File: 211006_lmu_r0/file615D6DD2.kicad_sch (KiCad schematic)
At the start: 26 parts, among them J11 Conn_ARM_JTAG_SWD_10, J12 Conn_01x03, SW1 SW_Push, SW2 SW_SPST, U9 STM32F103C8Tx, Y1 16MHz

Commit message: Updated lmu project with relative library paths and fixed broken symbols
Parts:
- FB1: symbol Device:Ferrite_Bead -> Device:FerriteBead
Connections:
- net +3V3: now reaches C183.1, C184.1, C185.1, C186.1, FB1.1, U9.1 (VBAT), U9.24 (VDD), U9.36 (VDD), U9.48 (VDD)
- net +3V3: now also J11.1 (VTref), R247.1
- net GND: now reaches U9.23 (VSS), U9.35 (VSS), U9.47 (VSS), U9.8 (VSSA)
- net GND: now also C182.2, C183.2, C184.2, C185.2, C186.2, D40.1 (K), D41.1 (K), D42.1 (K), D43.1 (K), D44.1 (K), J11.3 (GND), J11.5 (GND), J11.9 (GNDDetect), J12.3 (Pin_3), SW1.1, SW2.1 (A), Y1.2, Y1.3
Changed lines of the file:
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@@
     (pin "9")
   )
-  (symbol (lib_id "Device:Ferrite_Bead") (at 179.07 60.96 270) (unit 1)
+  (symbol (lib_id "Device:FerriteBead") (at 179.07 60.96 270) (unit 1)
     (in_bom yes) (on_board yes)
     (property "Reference" "FB1" (id 0) (at 180.34 64.77 90))
@@
       (effects (font (size 1.27 1.27)) hide)
     )
+    (pin "1")
   )
   (symbol (lib_id "gnd_iso:GND_ISO") (at 74.93 144.78 0) (unit 1)
@@
       (effects (font (size 1.27 1.27)) hide)
     )
+    (pin "1")
   )
   (symbol (lib_id "gnd_iso:GND_ISO") (at 66.04 144.78 0) (unit 1)
@@
       (effects (font (size 1.27 1.27)) hide)
     )
+    (pin "1")
   )
   (symbol (lib_id "gnd_iso:GND_ISO") (at 55.88 144.78 0) (unit 1)
@@
       (effects (font (size 1.27 1.27)) hide)
     )
+    (pin "1")
   )
   (symbol (lib_id "gnd_iso:GND_ISO") (at 45.72 144.78 0) (unit 1)
@@
       (effects (font (size 1.27 1.27)) hide)
     )
+    (pin "1")
   )
   (symbol (lib_id "gnd_iso:GND_ISO") (at 120.65 77.47 0) (unit 1)
@@
       (effects (font (size 1.27 1.27)) hide)
     )
+    (pin "1")
   )
   (symbol (lib_id "gnd_iso:GND_ISO") (at 107.95 77.47 0) (unit 1)
@@
       (effects (font (size 1.27 1.27)) hide)
     )
+    (pin "1")
   )
   (symbol (lib_id "gnd_iso:GND_ISO") (at 85.09 76.2 0) (unit 1)
@@
       (effects (font (size 1.27 1.27)) hide)
     )
+    (pin "1")
   )
   (symbol (lib_id "gnd_iso:GND_ISO") (at 95.25 81.28 0) (unit 1)
@@
       (effects (font (size 1.27 1.27)) hide)
     )
+    (pin "1")
   )
   (symbol (lib_id "gnd_iso:GND_ISO") (at 191.77 64.77 0) (unit 1)
@@
       (effects (font (size 1.27 1.27)) hide)
     )
+    (pin "1")
   )
   (symbol (lib_id "gnd_iso:GND_ISO") (at 200.66 64.77 0) (unit 1)
@@
       (effects (font (size 1.27 1.27)) hide)
     )
+    (pin "1")
   )
   (symbol (lib_id "gnd_iso:GND_ISO") (at 209.55 64.77 0) (unit 1)
@@
       (effects (font (size 1.27 1.27)) hide)
     )
+    (pin "1")
   )
   (symbol (lib_id "gnd_iso:GND_ISO") (at 218.44 64.77 0) (unit 1)
@@
       (effects (font (size 1.27 1.27)) hide)
     )
+    (pin "1")
   )
   (symbol (lib_id "gnd_iso:GND_ISO") (at 34.29 52.07 0) (unit 1)
@@
       (effects (font (size 1.27 1.27)) hide)
     )
+    (pin "1")
   )
   (symbol (lib_id "gnd_iso:GND_ISO") (at 71.12 30.48 0) (unit 1)
@@
       (effects (font (size 1.27 1.27)) hide)
     )
+    (pin "1")
   )
   (symbol (lib_id "+3v3_iso:+3V3_ISO") (at 218.44 57.15 0) (unit 1)
@@
       (effects (font (size 1.27 1.27)) hide)
     )
+    (pin "1")
   )
   (symbol (lib_id "+3v3_iso:+3V3_ISO") (at 85.09 58.42 0) (unit 1)
@@
       (effects (font (size 1.27 1.27)) hide)
     )
+    (pin "1")
   )
   (symbol (lib_id "+3v3_iso:+3V3_ISO") (at 34.29 21.59 0) (unit 1)
@@
       (effects (font (size 1.27 1.27)) hide)
     )
+    (pin "1")
   )
   (symbol (lib_id "Device:C") (at 200.66 60.96 0) (unit 1)
@@
       (effects (font (size 1.27 1.27)) hide)
     )
+    (pin "1")
   )
 )

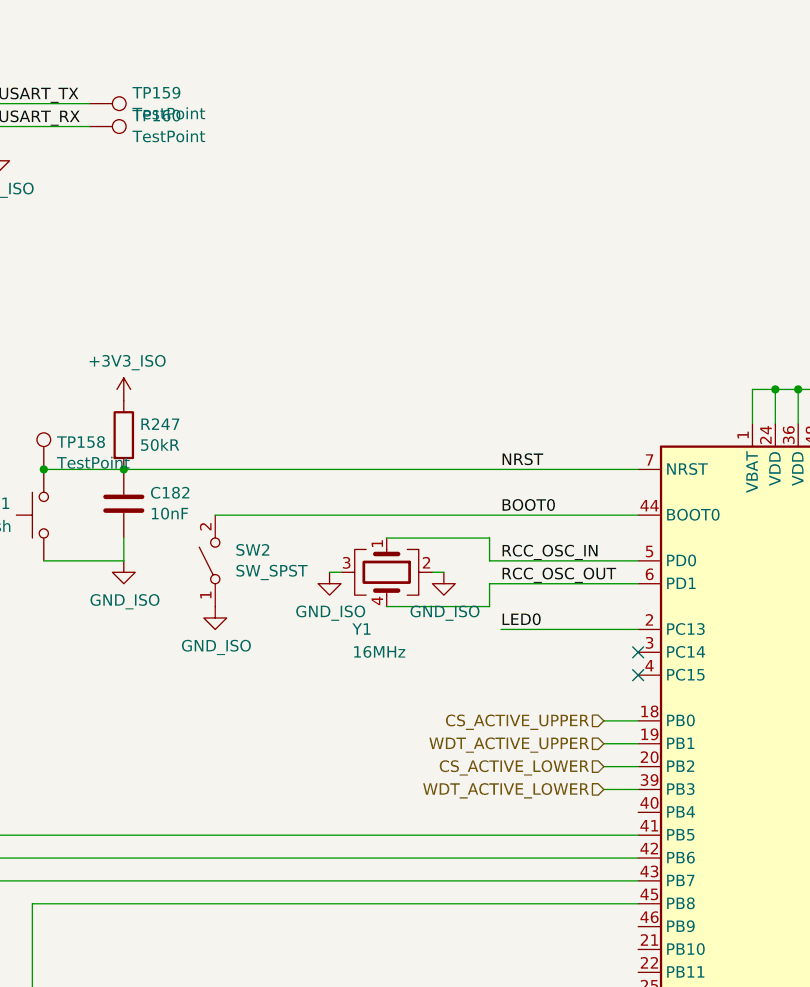
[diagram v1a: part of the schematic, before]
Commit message: Updated some components to make sourcing easier
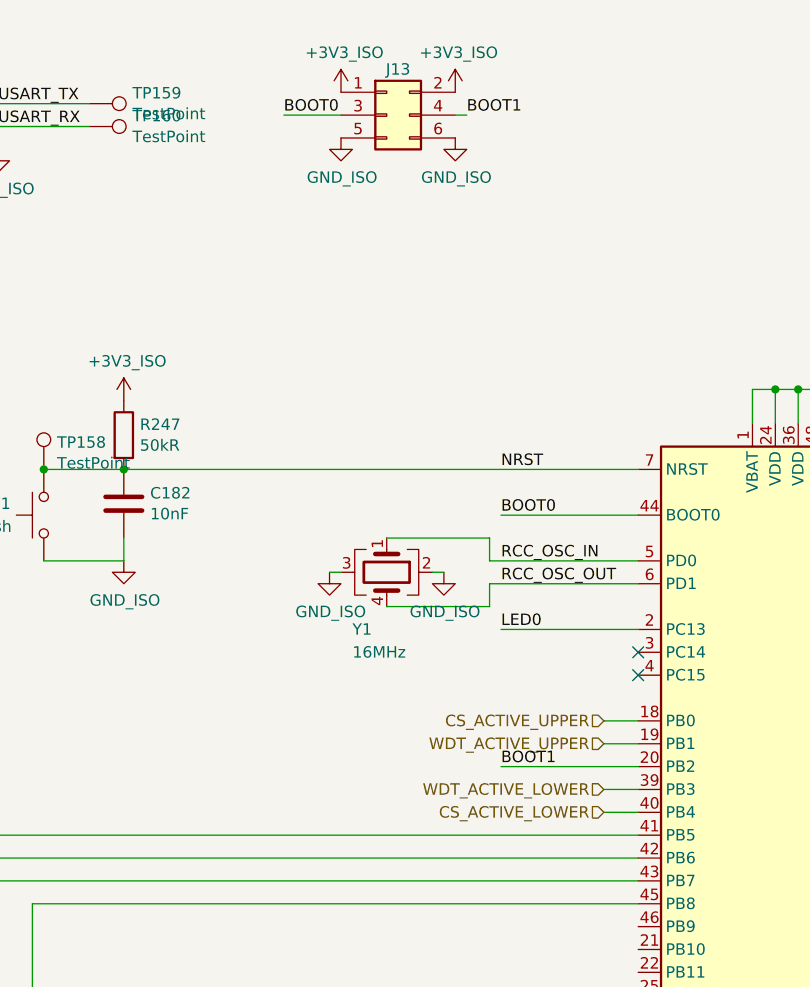
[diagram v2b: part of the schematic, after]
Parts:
- removed SW2: SW_SPST, Button_Switch_SMD:SW_DIP_SPSTx01_Slide_9.78x4.72mm_W8.61mm_P2.54mm, symbol Switch:SW_SPST
- added J13: Conn_02x03_Odd_Even, Connector_PinHeader_2.54mm:PinHeader_2x03_P2.54mm_Vertical, symbol Connector_Generic:Conn_02x03_Odd_Even
- C182, C183, C184, C185, C186, J12, R242, R243, R244, R245, R246, R247: Manufacturer (none) -> -; Part Number (none) -> -
- J11: Manufacturer (none) -> Samtec; Part Number (none) -> FTSH-105-01-L-DV-007-K
- SW1: footprint Button_Switch_SMD:SW_SPST_Omron_B3FS-100xP -> Button_Switch_SMD:SW_SPST_SKQG_WithStem; Manufacturer (none) -> XKB; Part Number (none) -> TS-1187A-C-D-B
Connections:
- net +3V3: now also J13.1 (Pin_1), J13.2 (Pin_2)
- net BOOT0: now also J13.3 (Pin_3)
- net CS_ACTIVE_LOWER: now also U9.40 (PB4); no longer U9.20 (PB2)
- net GND: now also J13.5 (Pin_5), J13.6 (Pin_6)
- new net BOOT1: J13.4 (Pin_4), U9.20 (PB2)

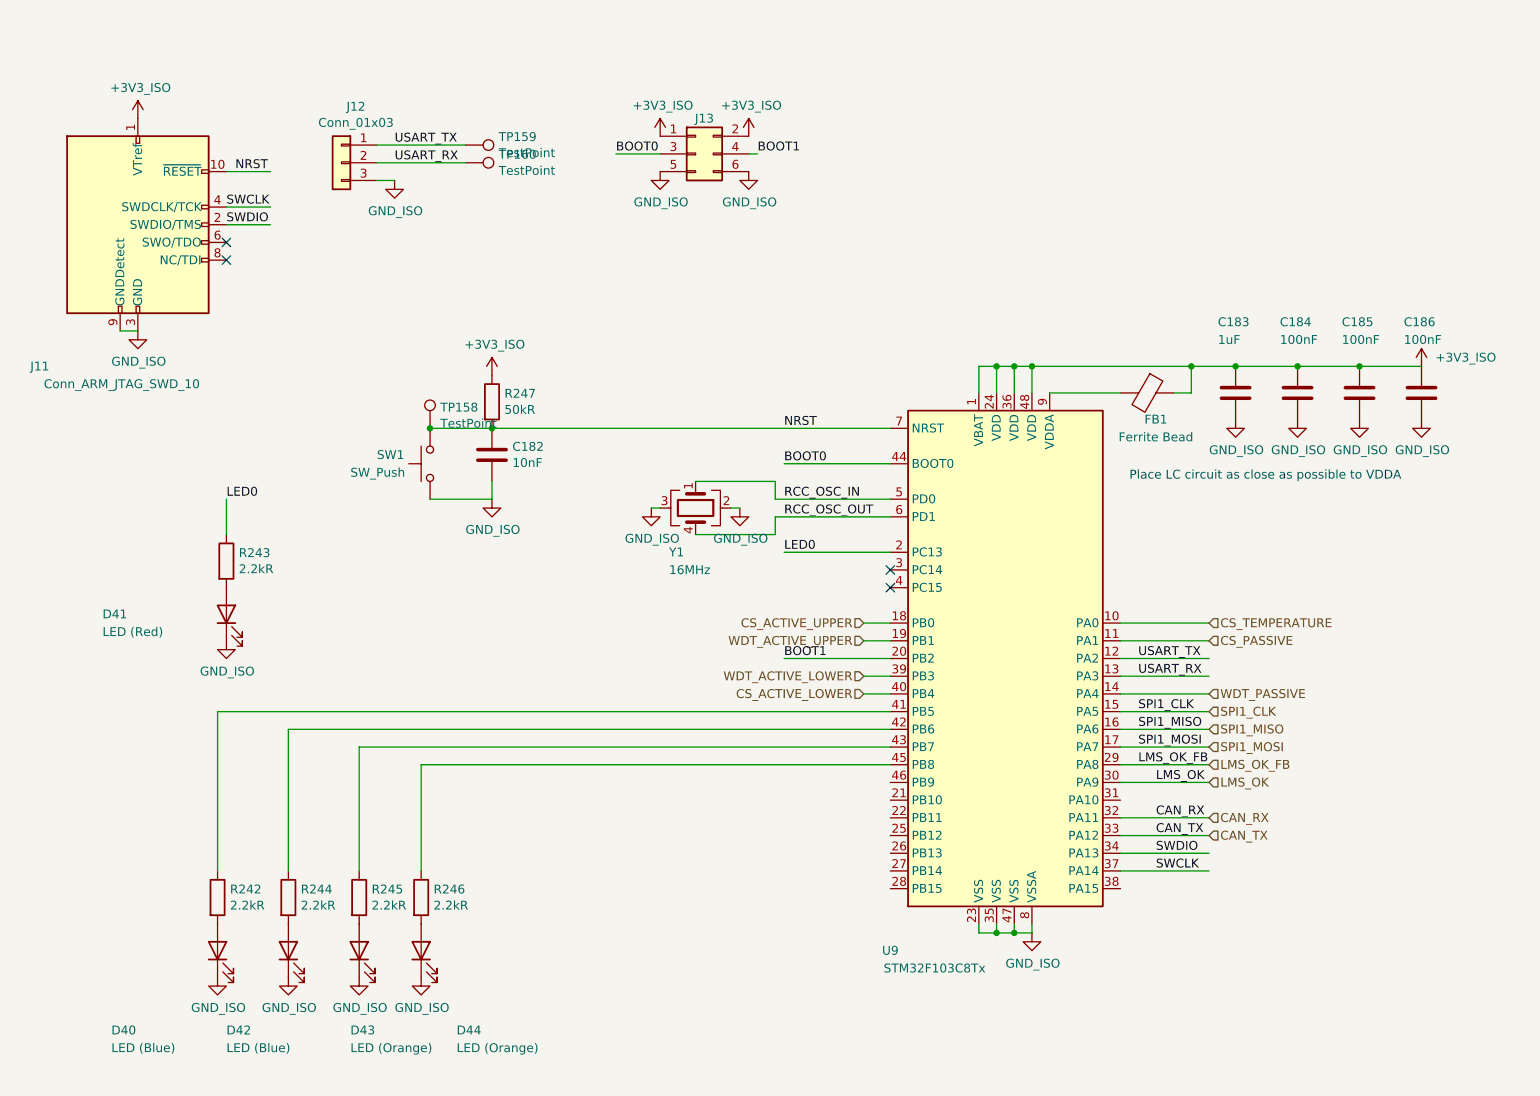
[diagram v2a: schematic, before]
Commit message: fixed footprints for headers, started planning out zones
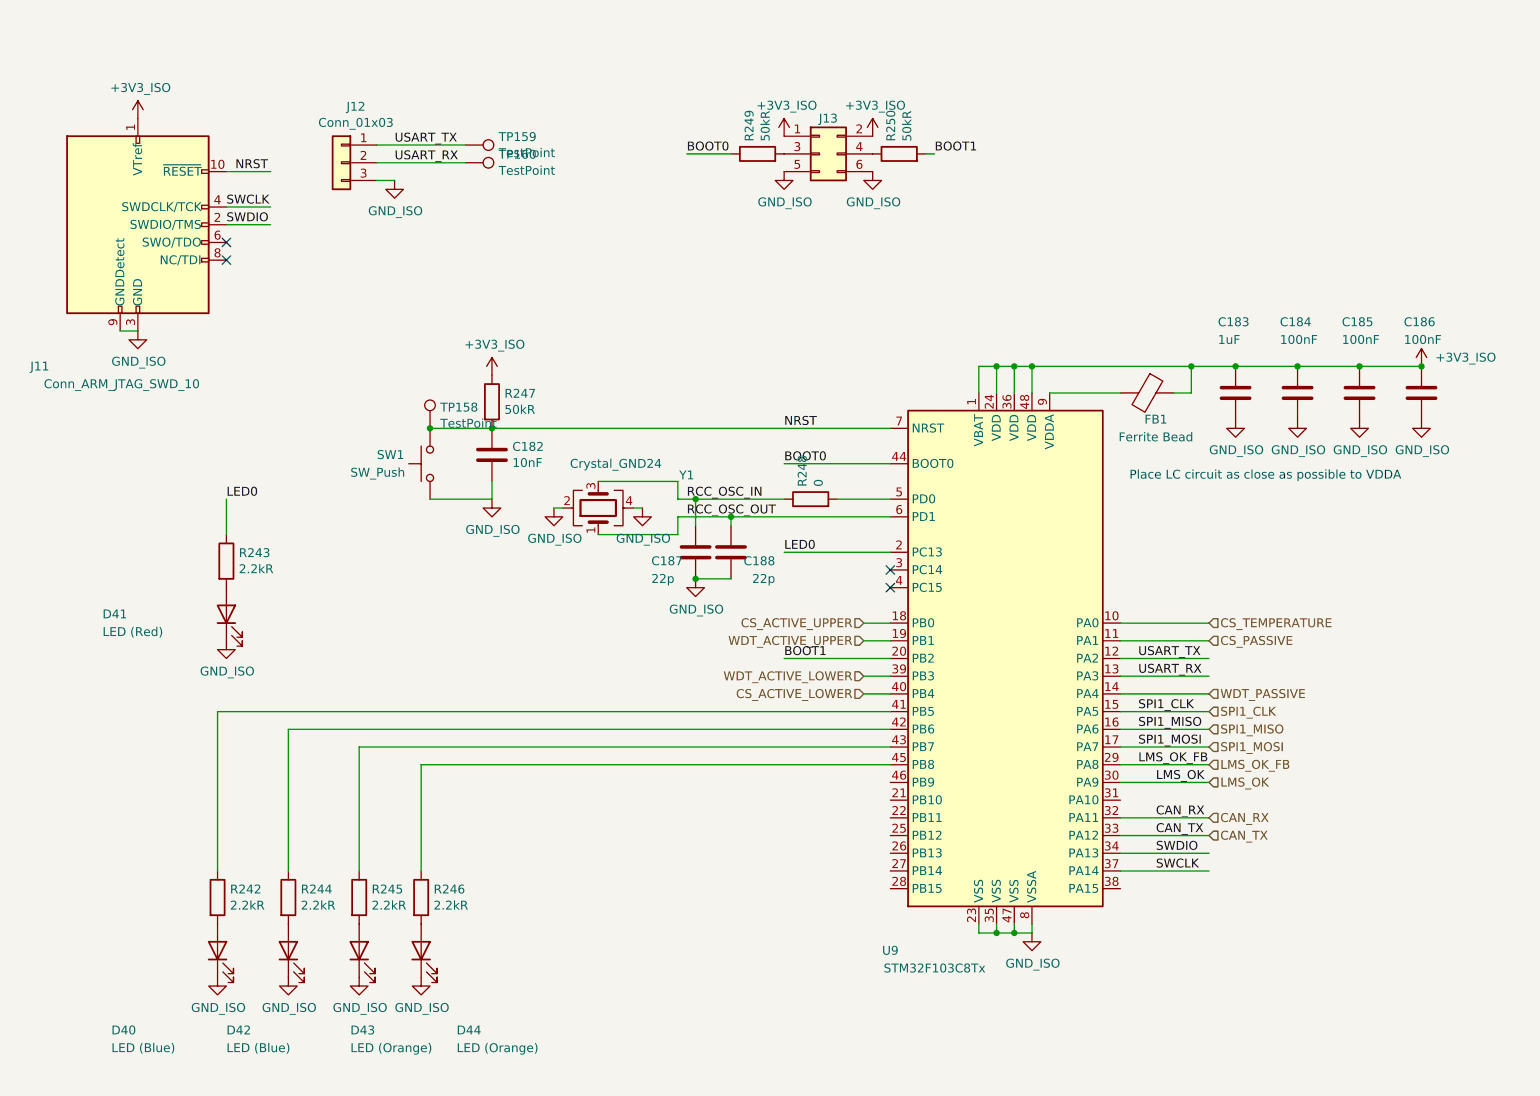
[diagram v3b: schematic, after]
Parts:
- removed Y1: 16MHz, Crystal:Crystal_SMD_3225-4Pin_3.2x2.5mm_HandSoldering, symbol Device:Crystal_GND23
- added C187, C188: 22p, Capacitor_SMD:C_0603_1608Metric_Pad1.08x0.95mm_HandSolder, symbol Device:C
- added R248: 0, Resistor_SMD:R_0603_1608Metric_Pad0.98x0.95mm_HandSolder, symbol Device:R
- added R249, R250: 50kR, Resistor_SMD:R_0603_1608Metric_Pad0.98x0.95mm_HandSolder, symbol Device:R
- added Y1: Crystal_GND24, Crystal:Crystal_SMD_3225-4Pin_3.2x2.5mm_HandSoldering, symbol Device:Crystal_GND24
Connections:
- net BOOT0: now also R249.1; no longer J13.3 (Pin_3)
- net BOOT1: now also R250.2; no longer J13.4 (Pin_4)
- net RCC_OSC_IN: now also C187.1, R248.1, Y1.3; no longer U9.5 (PD0)
- net RCC_OSC_OUT: now also C188.1, Y1.1
- net +3V3 renamed +3V3_ISO
- net GND renamed GND_ISO
- net GND_ISO: now also C187.2, C188.2, Y1.2, Y1.4
- new net: R248.2, U9.5 (PD0)
- new net: J13.3 (Pin_3), R249.2
- new net: J13.4 (Pin_4), R250.1
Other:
- moved on the sheet: J13

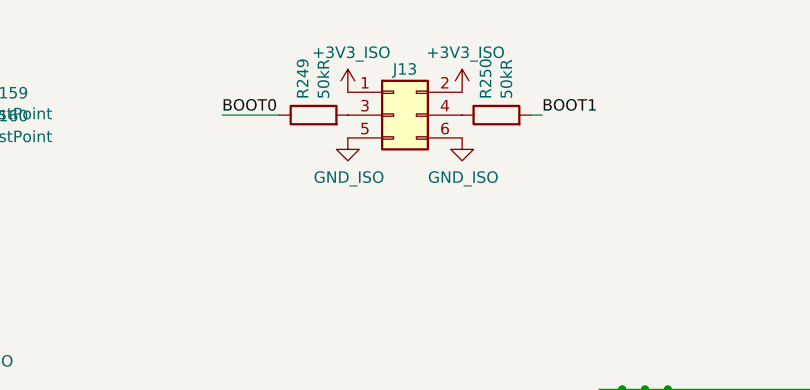
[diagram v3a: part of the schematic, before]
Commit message: updated pcb still need to find j11
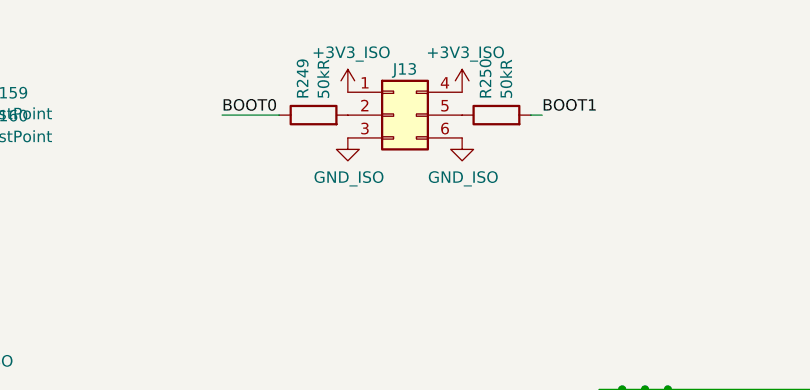
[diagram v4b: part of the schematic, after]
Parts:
- J13: symbol Connector_Generic:Conn_02x03_Odd_Even -> Connector_Generic:Conn_02x03_Top_Bottom
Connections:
- net +3V3_ISO: now also J13.4 (Pin_4); no longer J13.2 (Pin_2)
- net GND_ISO: now also J13.3 (Pin_3); no longer J13.5 (Pin_5)
- net at R249.2: now also J13.2 (Pin_2); no longer J13.3 (Pin_3)
- net at R250.1: now also J13.5 (Pin_5); no longer J13.4 (Pin_4)
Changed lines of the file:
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@@
     (pin "1")
   )
-  (symbol (lib_id "Connector_Generic:Conn_02x03_Odd_Even") (at 132.08 26.67 0) (unit 1)
+  (symbol (lib_id "Connector_Generic:Conn_02x03_Top_Bottom") (at 132.08 26.67 0) (unit 1)
     (in_bom yes) (on_board yes)
     (property "Reference" "J13" (id 0) (at 133.35 21.59 0))

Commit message: moved micro into position
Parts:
- J11: footprint Connector_PinHeader_1.27mm:PinHeader_2x09_P1.27mm_Vertical_SMD -> Connector_PinHeader_1.27mm:PinHeader_2x05_P1.27mm_Vertical_SMD
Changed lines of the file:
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@@
       (effects (font (size 1.27 1.27)) (justify right))
     )
-    (property "Footprint" "Connector_PinHeader_1.27mm:PinHeader_2x09_P1.27mm_Vertical_SMD" (id 2) (at 34.29 36.83 0)
+    (property "Footprint" "Connector_PinHeader_1.27mm:PinHeader_2x05_P1.27mm_Vertical_SMD" (id 2) (at 34.29 36.83 0)
       (effects (font (size 1.27 1.27)) hide)
     )
